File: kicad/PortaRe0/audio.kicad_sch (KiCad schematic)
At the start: 47 parts, among them J2 SPK_R, J3 SPK_L, U11 RP2040#2, U13 PCM5102APWR, U14 TPA6132A2RTER, U15 MAX98357AEWL+T_R, U9 MAX98357AEWL+T_L, Y3 12Mhz

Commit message: KiCad/Docs: チェックシート04-06完了・回路修正(session25)
- VL812: W25Q32 /CS GNDプルダウン→3V3_HUBプルアップ修正
- RP2040 #1/#2: クリスタルシンボル GND23→GND24 修正
- RP2040 #1: GP24/GP25 接続追加
- チェックシート04(VL812)/05(RP2040 kbd)/06(RP2040 audio)記入完了

Co-Authored-By: Claude Sonnet 4.6 <noreply@anthropic.com>
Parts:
- removed Y3: 12Mhz, Crystal:Crystal_SMD_3225-4Pin_3.2x2.5mm, symbol Device:Crystal_GND23_Small
- added Y2: C70565, symbol Device:Crystal_GND24_Small
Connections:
- net GNDPWR: now also Y2.2, Y2.4
- net at C74.1, U11.20 (XIN): now also Y2.1
- net at C75.1, U11.21 (XOUT): now also Y2.3
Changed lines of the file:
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@@
 	)
 	(junction
-		(at 53.34 132.08)
-		(diameter 0)
-		(color 0 0 0 0)
-	)
-	(junction
-		(at 53.34 137.16)
-		(diameter 0)
-		(color 0 0 0 0)
-	)
-	(junction
 		(at 53.34 97.79)
 		(diameter 0)
@@
 	)
 	(junction
+		(at 45.72 132.08)
+		(diameter 0)
+		(color 0 0 0 0)
+	)
+	(junction
 		(at 92.71 66.04)
 		(diameter 0)
@@
 	)
 	(junction
+		(at 53.34 137.16)
+		(diameter 0)
+		(color 0 0 0 0)
+	)
+	(junction
 		(at 92.71 60.96)
 		(diameter 0)
@@
 	)
 	(junction
+		(at 53.34 132.08)
+		(diameter 0)
+		(color 0 0 0 0)
+	)
+	(junction
 		(at 76.2 60.96)
 		(diameter 0)
@@
 	(wire
 		(pts
+			(xy 55.88 129.54) (xy 45.72 129.54)
+		)
+		(stroke
+			(width 0)
+			(type default)
+		)
+	)
+	(wire
+		(pts
 			(xy 201.93 97.79) (xy 210.82 97.79)
 		)
@@
 	(wire
 		(pts
-			(xy 53.34 132.08) (xy 62.23 132.08)
-		)
-		(stroke
-			(width 0)
-			(type default)
-		)
-	)
-	(wire
-		(pts
 			(xy 110.49 41.91) (xy 110.49 44.45)
 		)
@@
 	(wire
 		(pts
+			(xy 53.34 132.08) (xy 62.23 132.08)
+		)
+		(stroke
+			(width 0)
+			(type default)
+		)
+	)
+	(wire
+		(pts
 			(xy 97.79 60.96) (xy 95.25 60.96)
 		)
@@
 	(wire
 		(pts
+			(xy 45.72 132.08) (xy 45.72 134.62)
+		)
+		(stroke
+			(width 0)
+			(type default)
+		)
+	)
+	(wire
+		(pts
 			(xy 48.26 149.86) (xy 52.07 149.86)
 		)
@@
 	(wire
 		(pts
-			(xy 67.31 39.37) (xy 78.74 39.37)
+			(xy 53.34 137.16) (xy 62.23 137.16)
 		)
 		(stroke
@@
 	(wire
 		(pts
-			(xy 76.2 66.04) (xy 81.28 66.04)
+			(xy 67.31 39.37) (xy 78.74 39.37)
 		)
 		(stroke
@@
 	(wire
 		(pts
-			(xy 187.96 87.63) (xy 194.31 87.63)
+			(xy 76.2 66.04) (xy 81.28 66.04)
 		)
 		(stroke
@@
 	(wire
 		(pts
-			(xy 128.27 88.9) (xy 125.73 88.9)
+			(xy 187.96 87.63) (xy 194.31 87.63)
 		)
 		(stroke
@@
 	(wire
 		(pts
-			(xy 45.72 134.62) (xy 45.72 132.08)
+			(xy 128.27 88.9) (xy 125.73 88.9)
 		)
 		(stroke
@@
 	(wire
 		(pts
+			(xy 45.72 129.54) (xy 45.72 132.08)
+		)
+		(stroke
+			(width 0)
+			(type default)
+		)
+	)
+	(wire
+		(pts
 			(xy 193.04 130.81) (xy 218.44 130.81)
 		)
@@
 	(wire
 		(pts
-			(xy 53.34 137.16) (xy 62.23 137.16)
-		)
-		(stroke
-			(width 0)
-			(type default)
-		)
-	)
-	(wire
-		(pts
 			(xy 73.66 60.96) (xy 76.2 60.96)
 		)
@@
 	(wire
 		(pts
+			(xy 55.88 134.62) (xy 55.88 129.54)
+		)
+		(stroke
+			(width 0)
+			(type default)
+		)
+	)
+	(wire
+		(pts
 			(xy 102.87 66.04) (xy 102.87 78.74)
 		)
@@
 	)
 	(symbol
+		(lib_id "Device:Crystal_GND24_Small")
+		(at 53.34 134.62 270)
+		(unit 1)
+		(exclude_from_sim no)
+		(in_bom yes)
+		(on_board yes)
+		(dnp no)
+		(property "Reference" "Y2"
+			(at 57.404 134.112 90)
+			(effects
+				(font
+					(size 1.27 1.27)
+				)
+			)
+		)
+		(property "Value" "C70565"
+			(at 58.928 135.636 90)
+			(effects
+				(font
+					(size 1.27 1.27)
+				)
+			)
+		)
+		(property "Footprint" ""
+			(at 53.34 134.62 0)
+			(effects
+				(font
+					(size 1.27 1.27)
+				)
+				(hide yes)
+			)
+		)
+		(property "Datasheet" "~"
+			(at 53.34 134.62 0)
+			(effects
+				(font
+					(size 1.27 1.27)
+				)
+				(hide yes)
+			)
+		)
+		(property "Description" "Four pin crystal, GND on pins 2 and 4, small symbol"
+			(at 53.34 134.62 0)
+			(effects
+				(font
+					(size 1.27 1.27)
+				)
+				(hide yes)
+			)
+		)
+		(pin "2"
+		)
+		(pin "1"
+		)
+		(pin "3"
+		)
+		(pin "4"
+		)
+		(instances
+			(project "PortaRe0"
+				(path "/479aadc4-f9a0-4ec2-b000-6a17237038f1/6f018b3a-f554-45a0-adb8-bf1e4994a5d2"
+					(reference "Y2")
+					(unit 1)
+				)
+			)
+		)
+	)
+	(symbol
 		(lib_id "power:GNDPWR")
 		(at 213.36 138.43 270)
@@
 					(unit 1)
 				)
-			)
-		)
-	)
-	(symbol
-		(lib_id "Device:Crystal_GND23_Small")
-		(at 53.34 134.62 270)
-		(unit 1)
-		(exclude_from_sim no)
-		(in_bom yes)
-		(on_board yes)
-		(dnp no)
-		(property "Reference" "Y3"
-			(at 52.07 134.62 90)
-			(effects
-				(font
-					(size 1.27 1.27)
-				)
-				(justify left)
-			)
-		)
-		(property "Value" "12Mhz"
-			(at 55.118 134.62 90)
-			(effects
-				(font
-					(size 1.27 1.27)
-				)
-				(justify left)
-			)
-		)
-		(property "Footprint" "Crystal:Crystal_SMD_3225-4Pin_3.2x2.5mm"
-			(at 53.34 134.62 0)
-			(effects
-				(font
-					(size 1.27 1.27)
-				)
-				(hide yes)
-			)
-		)
-		(property "Datasheet" "~"
-			(at 53.34 134.62 0)
-			(effects
-				(font
-					(size 1.27 1.27)
-				)
-				(hide yes)
-			)
-		)
-		(property "Description" "Four pin crystal, GND on pins 2 and 3, small symbol"
-			(at 43.18 134.62 0)
-			(effects
-				(font
-					(size 1.27 1.27)
-				)
-				(hide yes)
-			)
-		)
-		(property private "KLC_S4.1" "Some pins are on 50mil grid to make the symbol small"
-			(at 34.29 134.62 0)
-			(show_name yes)
-			(effects
-				(font
-					(size 1.27 1.27)
-				)
-				(hide yes)
-			)
-		)
-		(property private "KLC_S3.3" "The rectangle is not a symbol body but a graphical element"
-			(at 36.83 135.89 0)
-			(show_name yes)
-			(effects
-				(font
-					(size 1.27 1.27)
-				)
-				(hide yes)
-			)
-		)
-		(pin "4"
-		)
-		(pin "3"
-		)
-		(pin "1"
-		)
-		(pin "2"
-		)
-		(instances
-			(project "PortaRe0"
-				(path "/479aadc4-f9a0-4ec2-b000-6a17237038f1/6f018b3a-f554-45a0-adb8-bf1e4994a5d2"
-					(reference "Y3")
-					(unit 1)
-				)

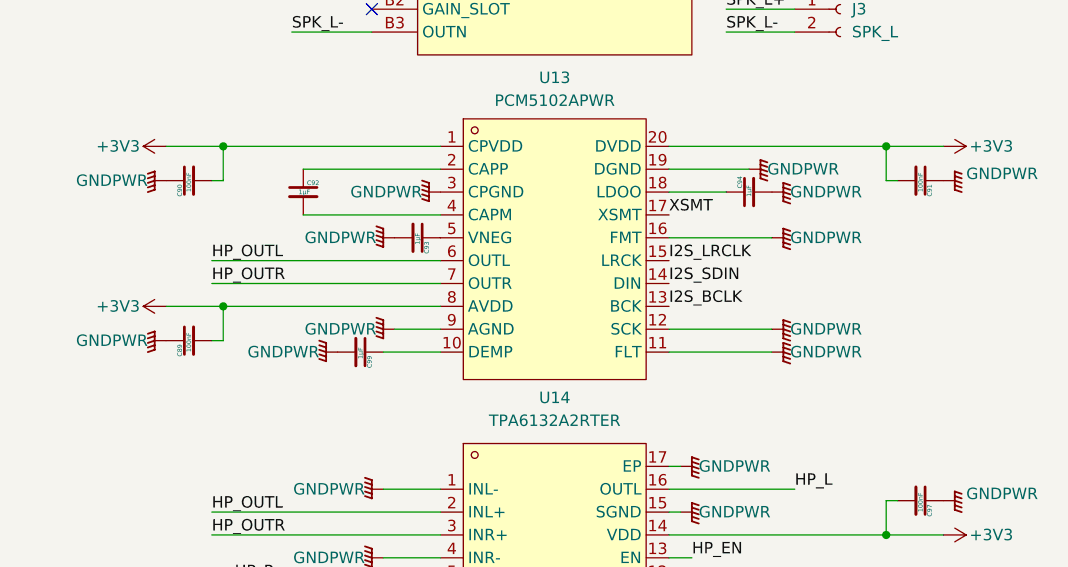
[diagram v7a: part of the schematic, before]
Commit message: KiCad/Docs: audioシートバイパスキャップ追加・MAX98357Aチェックシート更新
- audio.kicad_sch: MAX98357A (U9/U15) VDDバイパスキャップ C115/C116 (10µF) 追加
- audio.kicad_sch: C99値 1µF→10µF、他コンデンサ値更新、GNDPWRシンボル移動
- 07_MAX98357A_checklist.txt: ピン確認結果記入 (ok/? マーク)
- CONTEXT.md: BOM更新・整合チェック行テキスト修正

Co-Authored-By: Claude Sonnet 4.6 <noreply@anthropic.com>
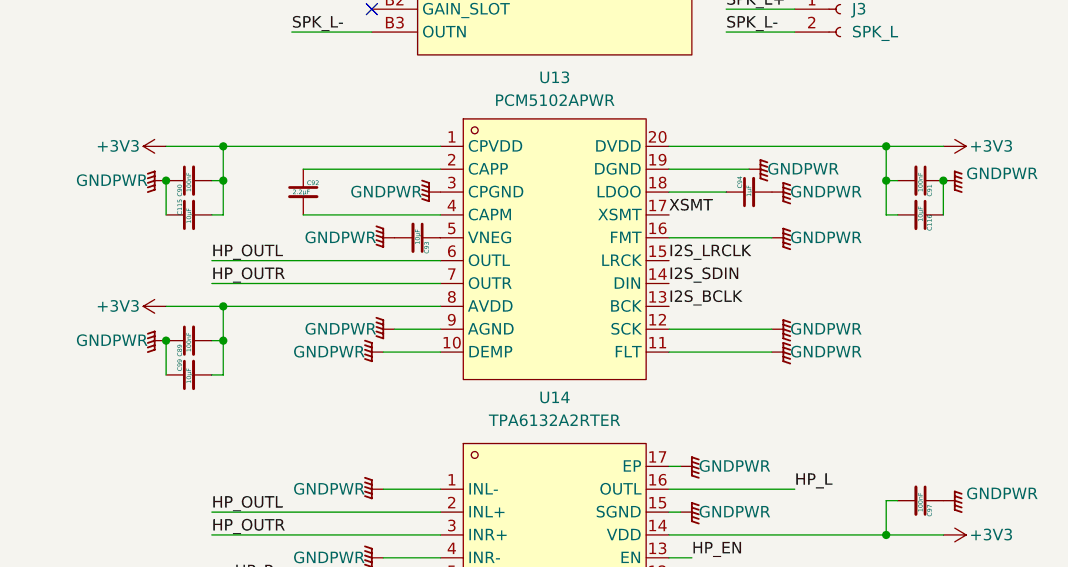
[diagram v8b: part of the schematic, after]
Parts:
- added C115, C116: 10μF, symbol Device:C_Small
- C92: value 1μF -> 2.2μF
- C93, C99: value 1μF -> 10μF
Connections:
- net +3V3: now also C99.2, C115.2, C116.2
- net GNDPWR: now also C99.1, U13.10 (DEMP), C115.1, C116.1; no longer C99.2
